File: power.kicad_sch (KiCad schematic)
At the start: 27 parts, among them J3 Conn_01x03_Male, Q1 DMP1045U-7, Q2 UMW8205A, U1 XC6210B332MR, U2 TP4056M, U3 DW01A-G, U4 MAX17048G+T10

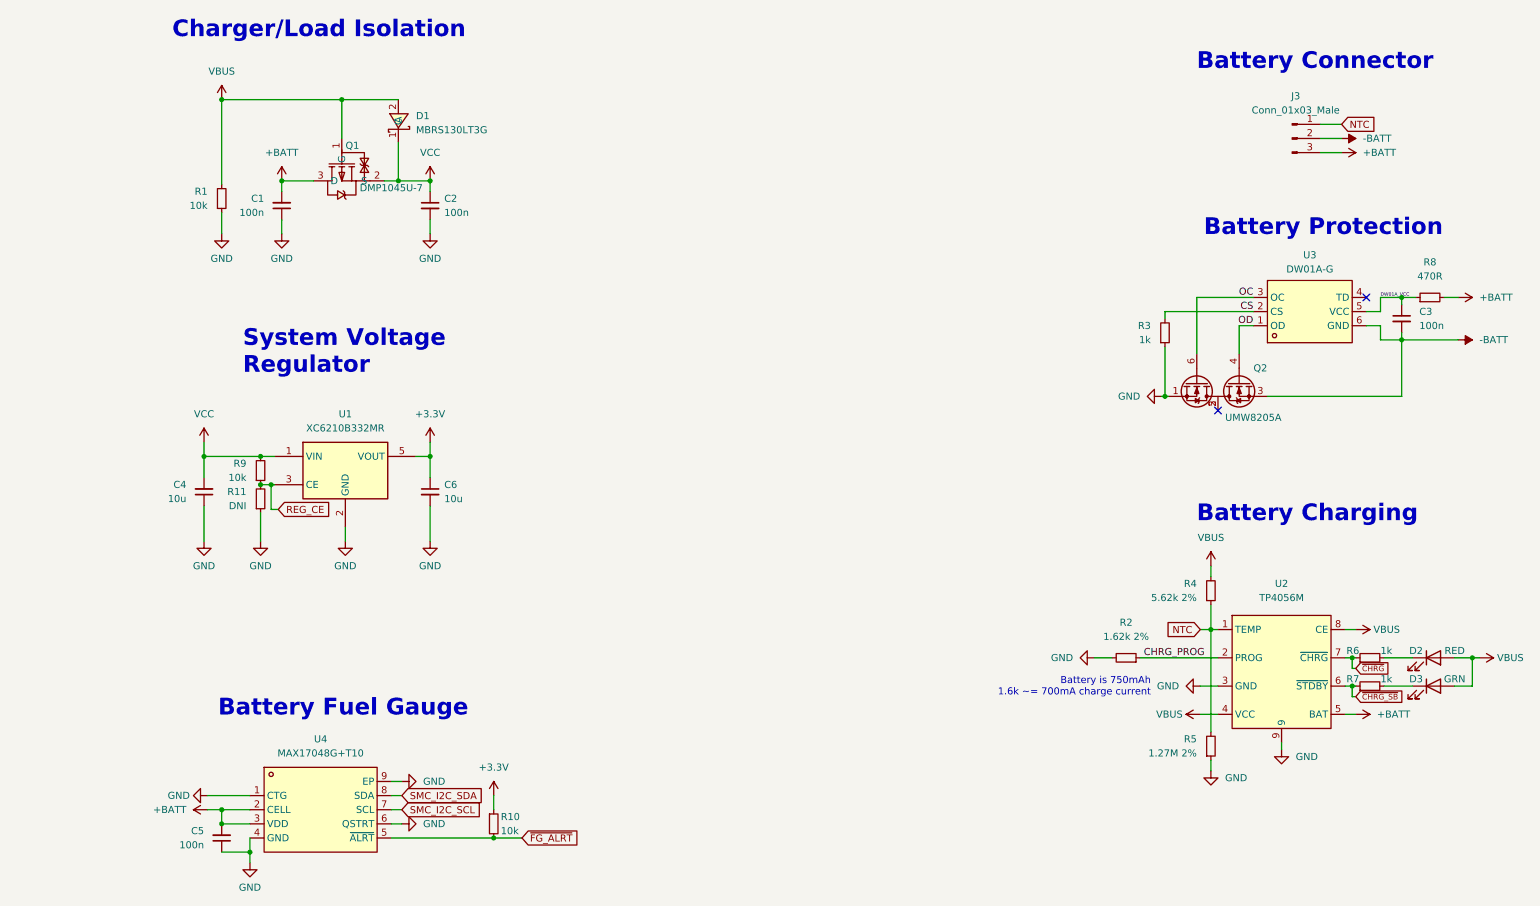
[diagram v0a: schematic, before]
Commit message: layout: preliminary layout of most of board
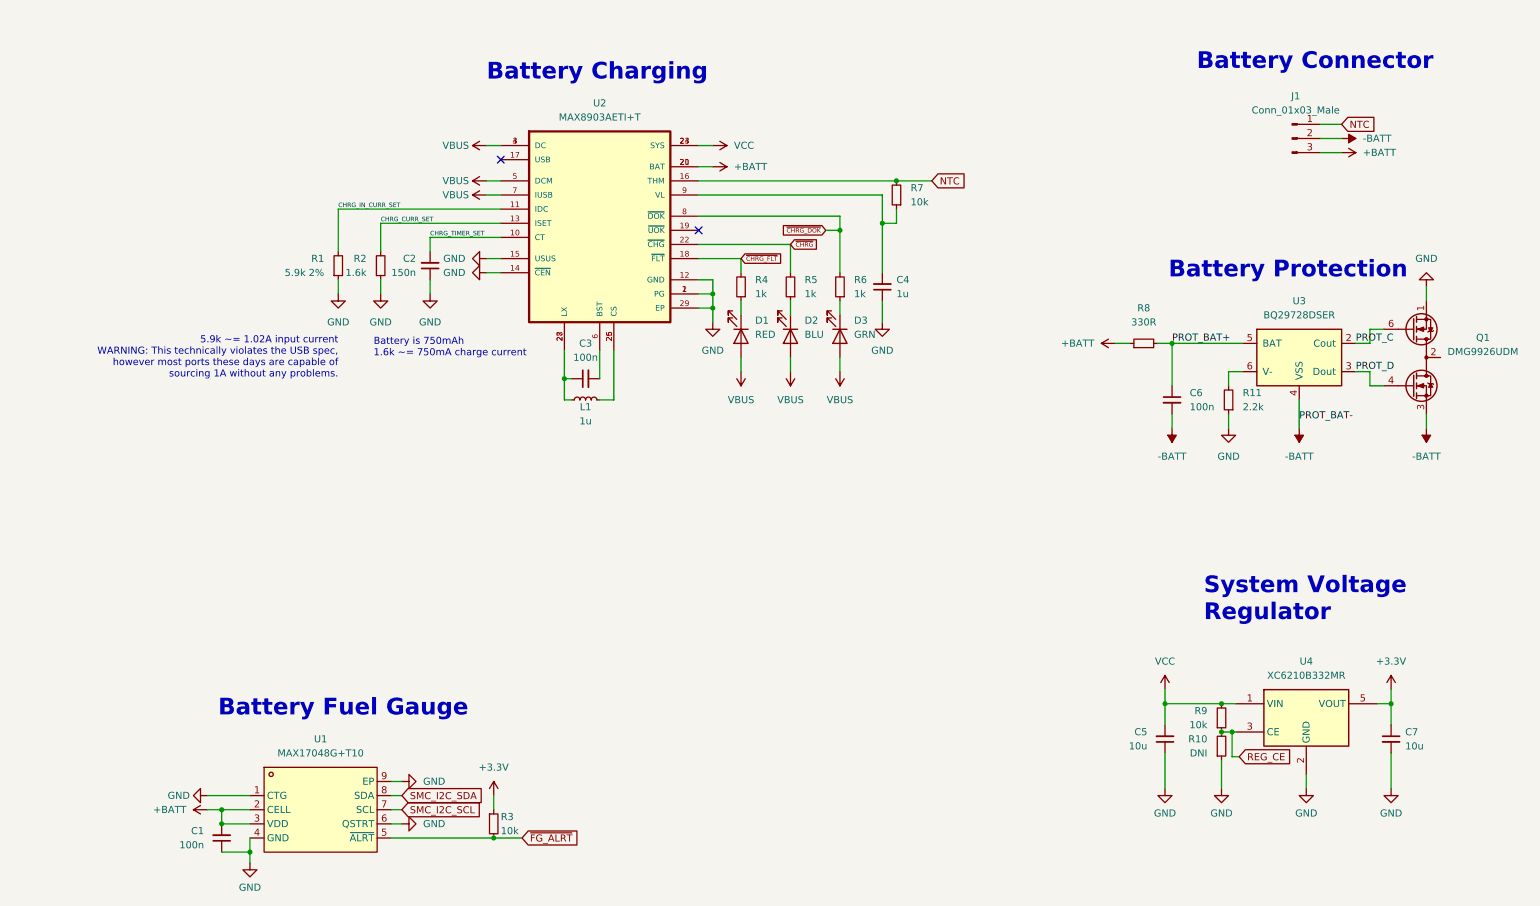
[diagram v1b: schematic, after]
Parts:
- removed C1: 100n, Capacitor_SMD:C_0402_1005Metric, symbol Device:C_Small
- removed D1: MBRS130LT3G, Diode_SMD:D_SMB, symbol lcsc:MBRS130LT3G
- removed Q1: DMP1045U-7, Package_TO_SOT_SMD:SOT-23, symbol lcsc:DMP1045U-7
- removed Q2: UMW8205A, Package_TO_SOT_SMD:SOT-23-6, symbol lcsc:UMW8205A
- removed R3: 1k, Resistor_SMD:R_0402_1005Metric, symbol Device:R_Small
- removed U2: TP4056M, Gigahawk:MSOP-8-1EP_3x3mm_P0.65mm_EP1.425x1.76mm, symbol lcsc:TP4056M
- removed U3: DW01A-G, Package_TO_SOT_SMD:SOT-23-6, symbol lcsc:DW01A-G
- added C4: 1u, Capacitor_SMD:C_0402_1005Metric, symbol Device:C_Small
- added C6: 100n, Capacitor_SMD:C_0402_1005Metric, symbol Device:C_Small
- added D1: RED, LED_SMD:LED_0402_1005Metric, symbol Device:LED
- added L1: 1u, Inductor_SMD:L_Vishay_IFSC-1515AH_4x4x1.8mm, symbol Device:L_Small
- added Q1: DMG9926UDM, Package_TO_SOT_SMD:SOT-23-6, symbol Transistor_FET:DMG9926UDM
- added R11: 2.2k, Resistor_SMD:R_0402_1005Metric, symbol Device:R_Small
- added U2: MAX8903AETI+T, Package_DFN_QFN:QFN-28-1EP_4x4mm_P0.4mm_EP2.6x2.6mm, symbol gigahawk:MAX8903AETI+T
- added U3: BQ29728DSER, Package_SON:WSON-6_1.5x1.5mm_P0.5mm, symbol Battery_Management:BQ297xy
- C2: value 100n -> 150n
- D2: value RED -> BLU; footprint LED_SMD:LED_0201_0603Metric -> LED_SMD:LED_0402_1005Metric
- D3: footprint LED_SMD:LED_0201_0603Metric -> LED_SMD:LED_0402_1005Metric
- R1: value 10k -> 5.9k 2%
- R2: value 1.62k 2% -> 1.6k
- R4: value 5.62k 2% -> 1k
- R5: value 1.27M 2% -> 1k
- R7: value 1k -> 10k
- R8: value 470R -> 330R
- renumbered C5 to C1, C4 to C5, C6 to C7, J3 to J1, R11 to R10, R10 to R3, U4 to U1, U1 to U4
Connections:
- net CHRG_PROG is gone; now on net GND: R2.1
- net +BATT: now also R8.1, U2.20 (BAT), U2.21 (BAT); no longer R8.2
- net -BATT: now also C6.2, Q1.3 (S2), U3.4 (VSS); no longer C3.2
- net GND: now also C2.1, C4.1, Q1.1 (D1), R11.1, U2.1 (PG), U2.12 (GND), U2.14 (~{CEN}), U2.15 (USUS), U2.2 (PG), U2.29 (EP); no longer C2.2, R2.2, R5.1
- net NTC: now also R7.2, U2.16 (THM); no longer R4.1, R5.2
- net VBUS: now also D1.2 (A), U2.3 (DC), U2.4 (DC), U2.5 (DCM), U2.7 (IUSB); no longer R1.2, R4.2
- net VCC: now also U2.23 (SYS), U2.24 (SYS); no longer C2.1
- net ~{CHRG}: now also R5.2, U2.22 (~{CHG}); no longer R6.1
- net at D2.1 (K): now also R5.1; no longer R6.2
- net at D3.1 (K): now also R6.1; no longer R7.2
- net DW01A_VCC: no longer names the net of C3.1
- net DW01A_VCC: now also L1.2, U2.27 (LX), U2.28 (LX); no longer R8.1
- net ~{CHRG_SB}: no longer names the net of R7.1
- net ~{CHRG_SB}: now also C4.2, U2.9 (VL)
- new net: D1.1 (K), R4.1
- new net: Q1.2 (S1/D2), Q1.5 (S1/D2)
- new net: R11.2, U3.6 (V-)
- new net: L1.1, U2.25 (CS), U2.26 (CS)
- new net: C3.2, U2.6 (BST)
- new net CHRG_CURR_SET: R2.2, U2.13 (ISET)
- new net CHRG_IN_CURR_SET: R1.2, U2.11 (IDC)
- new net CHRG_TIMER_SET: C2.2, U2.10 (CT)
- new net PROT_BAT+: C6.1, R8.2, U3.5 (BAT)
- new net PROT_C: Q1.6 (G1), U3.2 (Cout)
- new net PROT_D: Q1.4 (G2), U3.3 (Dout)
- new net ~{CHRG_DOK}: R6.2, U2.8 (~{DOK})
- new net ~{CHRG_FLT}: R4.2, U2.18 (~{FLT})
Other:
- note added: "5.9k ~= 1.02A input current WARNING: This technically violates the USB spec, however most ports these days are capable of sourcing 1A without any problems."
- note added: "Battery is 750mAh 1.6k ~= 750mA charge current"
- note removed: "Battery is 750mAh 1.6k ~= 700mA charge current"
- note removed: "Charger/Load Isolation"
- moved on the sheet: C5, C7, R10, R9, U4

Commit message: layout, routing: relayout and reroute board
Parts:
- C1, C3, C6: value 100n -> (none); footprint Capacitor_SMD:C_0402_1005Metric -> (none)
- C2: value 150n -> (none); footprint Capacitor_SMD:C_0402_1005Metric -> (none)
- C4: value 1u -> (none); footprint Capacitor_SMD:C_0402_1005Metric -> (none)
- C5, C7: value 10u -> (none); footprint Capacitor_SMD:C_0402_1005Metric -> (none)
- D1: value RED -> (none); footprint LED_SMD:LED_0402_1005Metric -> (none)
- D2: value BLU -> (none); footprint LED_SMD:LED_0402_1005Metric -> (none)
- D3: value GRN -> (none); footprint LED_SMD:LED_0402_1005Metric -> (none)
- J1: value Conn_01x03_Male -> (none); footprint Gigahawk:Molex_PicoBlade_53047-0310_1x03_P1.25mm_Vertical -> (none)
- L1: value 1u -> (none); footprint Inductor_SMD:L_Vishay_IFSC-1515AH_4x4x1.8mm -> (none)
- Q1: value DMG9926UDM -> (none); footprint Package_TO_SOT_SMD:SOT-23-6 -> (none)
- R1: value 5.9k 2% -> (none); footprint Resistor_SMD:R_0402_1005Metric -> (none)
- R10: value DNI -> (none); footprint Resistor_SMD:R_0402_1005Metric -> (none)
- R11: value 2.2k -> (none); footprint Resistor_SMD:R_0402_1005Metric -> (none)
- R2: value 1.6k -> (none); footprint Resistor_SMD:R_0402_1005Metric -> (none)
- R3, R7, R9: value 10k -> (none); footprint Resistor_SMD:R_0402_1005Metric -> (none)
- R4, R5, R6: value 1k -> (none); footprint Resistor_SMD:R_0402_1005Metric -> (none)
- R8: value 330R -> (none); footprint Resistor_SMD:R_0402_1005Metric -> (none)
- U1: value MAX17048G+T10 -> (none); footprint Package_DFN_QFN:DFN-8-1EP_2x2mm_P0.5mm_EP0.6x1.2mm -> (none)
- U2: value MAX8903AETI+T -> (none); footprint Package_DFN_QFN:QFN-28-1EP_4x4mm_P0.4mm_EP2.6x2.6mm -> (none)
- U3: value BQ29728DSER -> (none); footprint Package_SON:WSON-6_1.5x1.5mm_P0.5mm -> (none)
- U4: value XC6210B332MR -> (none); footprint Package_TO_SOT_SMD:SOT-23-5 -> (none)
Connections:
- net CHRG_VL: now reaches C4.2, R7.1, U2.9 (VL)
- net CHRG_FLT_LEDK: now reaches D1.1 (K), R4.1
- net at Q1.2 (S1/D2): no longer Q1.5 (S1/D2)
- net PROT_V-: now reaches R11.2, U3.6 (V-)
- net CHRG_CS: now reaches L1.1, U2.25 (CS), U2.26 (CS)
- net CHRG_LX: now reaches C3.1, L1.2, U2.27 (LX), U2.28 (LX)
- net CHRG_BST: now reaches C3.2, U2.6 (BST)
- net CHRG_LEDK: now reaches D2.1 (K), R5.1
- net CHRG_DOK_LEDK: now reaches D3.1 (K), R6.1
- no-connect marks 2 -> 4

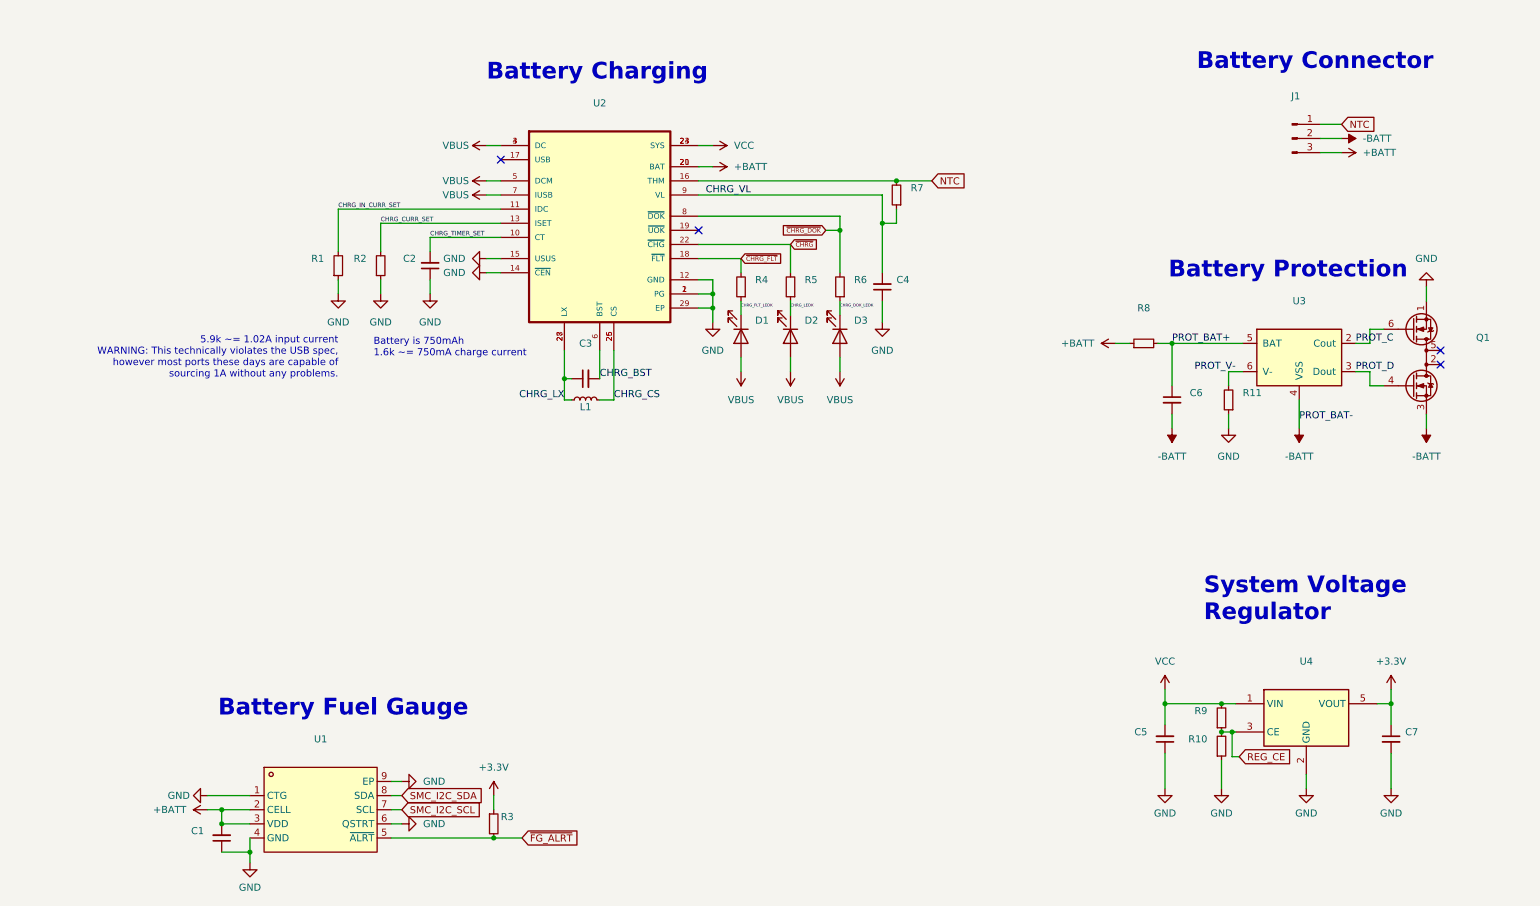
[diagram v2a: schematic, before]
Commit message: layout: add testpoints, extra mounting hole, grounding clips
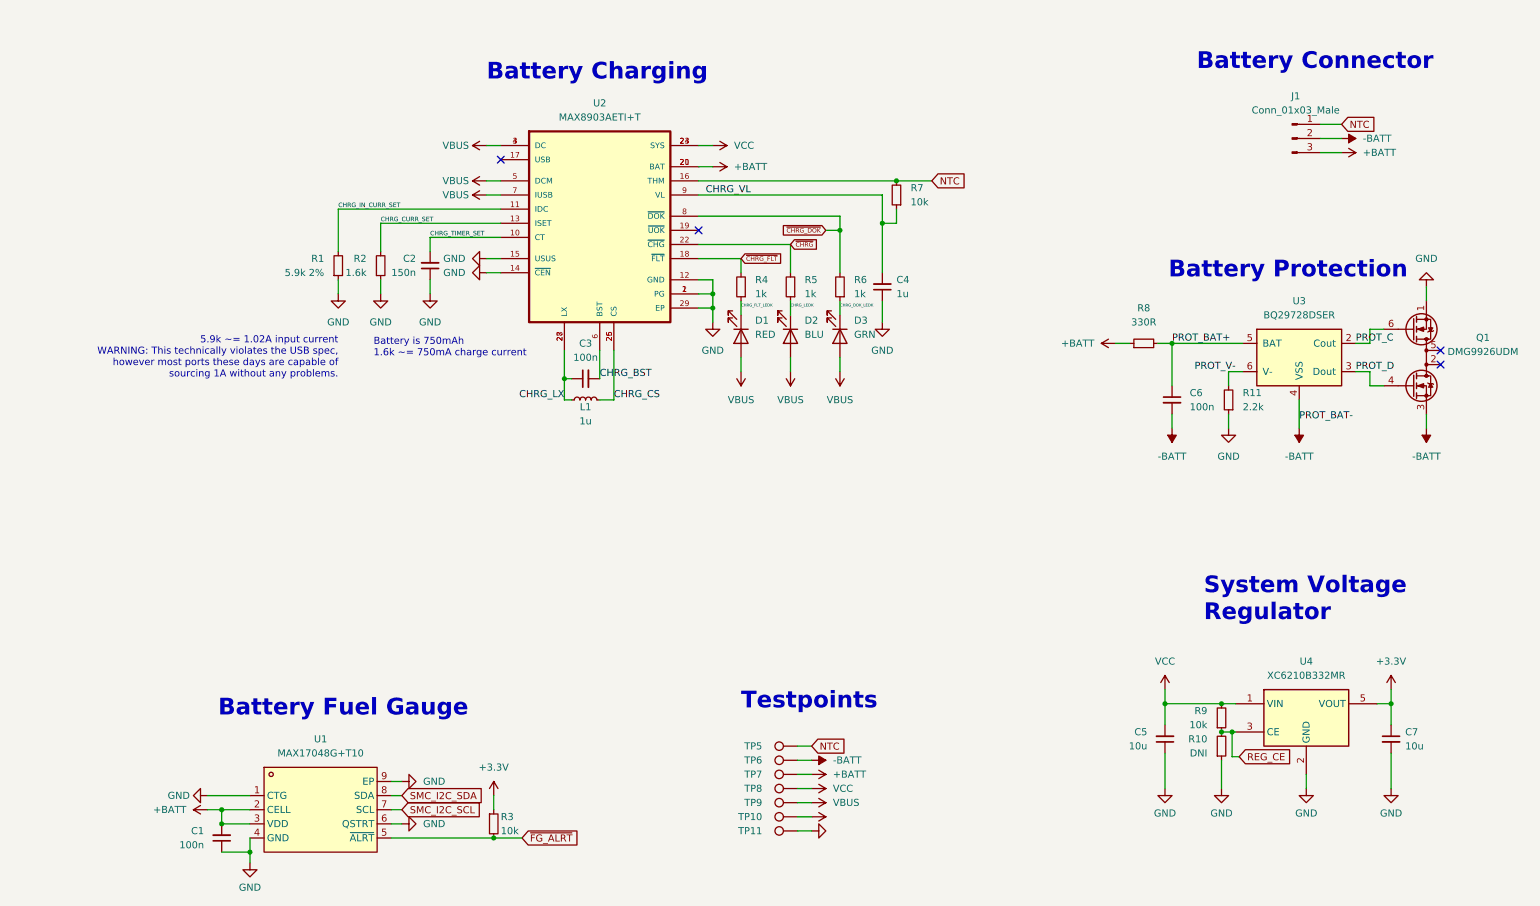
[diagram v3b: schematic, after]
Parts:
- added TP10, TP11, TP5, TP6, TP7, TP8, TP9: TestPoint, TestPoint:TestPoint_Pad_D1.5mm, symbol Connector:TestPoint
- C1, C3, C6: value (none) -> 100n; footprint (none) -> Capacitor_SMD:C_0402_1005Metric
- C2: value (none) -> 150n; footprint (none) -> Capacitor_SMD:C_0402_1005Metric
- C4: value (none) -> 1u; footprint (none) -> Capacitor_SMD:C_0402_1005Metric
- C5, C7: value (none) -> 10u; footprint (none) -> Capacitor_SMD:C_0402_1005Metric
- D1: value (none) -> RED; footprint (none) -> LED_SMD:LED_0402_1005Metric
- D2: value (none) -> BLU; footprint (none) -> LED_SMD:LED_0402_1005Metric
- D3: value (none) -> GRN; footprint (none) -> LED_SMD:LED_0402_1005Metric
- J1: value (none) -> Conn_01x03_Male; footprint (none) -> Gigahawk:Molex_PicoBlade_53047-0310_1x03_P1.25mm_Vertical
- L1: value (none) -> 1u; footprint (none) -> Inductor_SMD:L_Vishay_IFSC-1515AH_4x4x1.8mm
- Q1: value (none) -> DMG9926UDM; footprint (none) -> Package_TO_SOT_SMD:SOT-23-6
- R1: value (none) -> 5.9k 2%; footprint (none) -> Resistor_SMD:R_0402_1005Metric
- R10: value (none) -> DNI; footprint (none) -> Resistor_SMD:R_0402_1005Metric
- R11: value (none) -> 2.2k; footprint (none) -> Resistor_SMD:R_0402_1005Metric
- R2: value (none) -> 1.6k; footprint (none) -> Resistor_SMD:R_0402_1005Metric
- R3, R7, R9: value (none) -> 10k; footprint (none) -> Resistor_SMD:R_0402_1005Metric
- R4, R5, R6: value (none) -> 1k; footprint (none) -> Resistor_SMD:R_0402_1005Metric
- R8: value (none) -> 330R; footprint (none) -> Resistor_SMD:R_0402_1005Metric
- U1: value (none) -> MAX17048G+T10; footprint (none) -> Package_DFN_QFN:DFN-8-1EP_2x2mm_P0.5mm_EP0.6x1.2mm
- U2: value (none) -> MAX8903AETI+T; footprint (none) -> Package_DFN_QFN:QFN-28-1EP_4x4mm_P0.4mm_EP2.6x2.6mm
- U3: value (none) -> BQ29728DSER; footprint (none) -> Package_SON:WSON-6_1.5x1.5mm_P0.5mm
- U4: value (none) -> XC6210B332MR; footprint (none) -> Package_TO_SOT_SMD:SOT-23-5
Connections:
- net +3V3: now also TP10.1
- net +BATT: now also TP7.1
- net -BATT: now also TP6.1
- net GND: now also TP11.1
- net NTC: now also TP5.1
- net VBUS: now also TP9.1
- net VCC: now also TP8.1
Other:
- note added: "Testpoints"

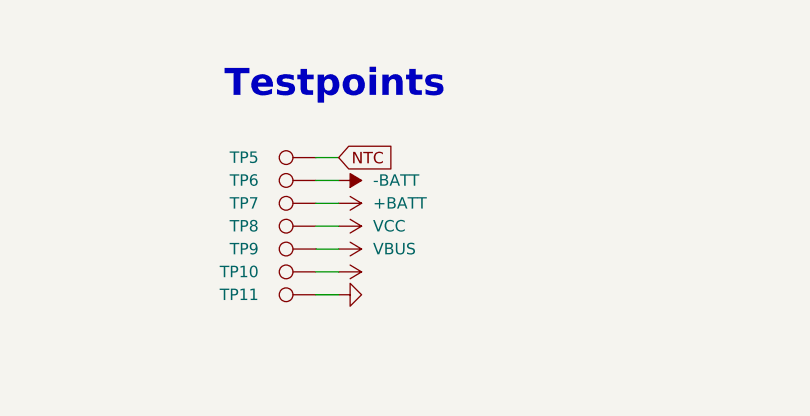
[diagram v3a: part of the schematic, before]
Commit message: layout: cleanup silkscreen, add bootloader buttons
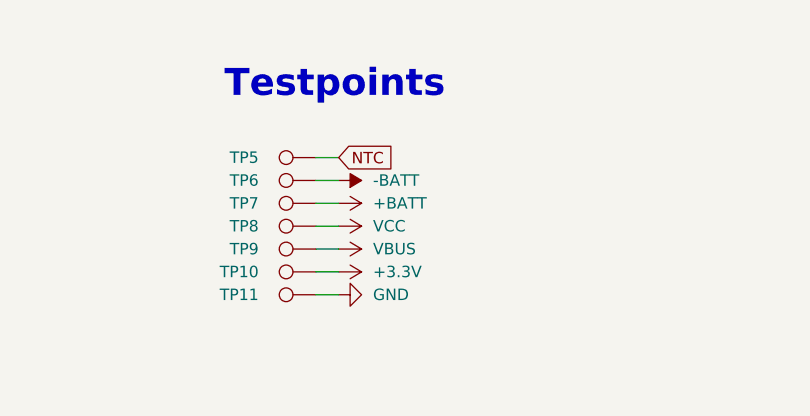
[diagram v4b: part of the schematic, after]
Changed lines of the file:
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@@
       (effects (font (size 1.27 1.27)) hide)
     )
-    (property "Value" "" (id 1) (at 154.94 161.2899 90)
+    (property "Value" "+3.3V" (id 1) (at 154.94 161.2899 90)
       (effects (font (size 1.27 1.27)) (justify left))
     )
@@
       (effects (font (size 1.27 1.27)) hide)
     )
-    (property "Value" "" (id 1) (at 154.94 163.8299 90)
-      (effects (font (size 1.27 1.27)) (justify right))
-    )
+    (property "Value" "GND" (id 1) (at 154.94 163.8299 90)
+      (effects (font (size 1.27 1.27)) (justify right))
+    )
